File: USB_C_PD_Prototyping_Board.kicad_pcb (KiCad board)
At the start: 2 copper layers, 60 x 45 mm, 48 parts, among them IC1 TPS259474LRPWR, IC2 BD33FC0FP-E2, J1 USB_C_Receptacle, J2 Power_out, J3 Data_out, J5 Conn_01x04_Pin, J6 Conn_02x02_Counter_Clockwise, J7 Conn_02x02_Counter_Clockwise, Q1 DMP3018SFV-7, Q2 DMP3018SFV-7, SW1 Power_out_switch, U1 HUSB238_xxxDD

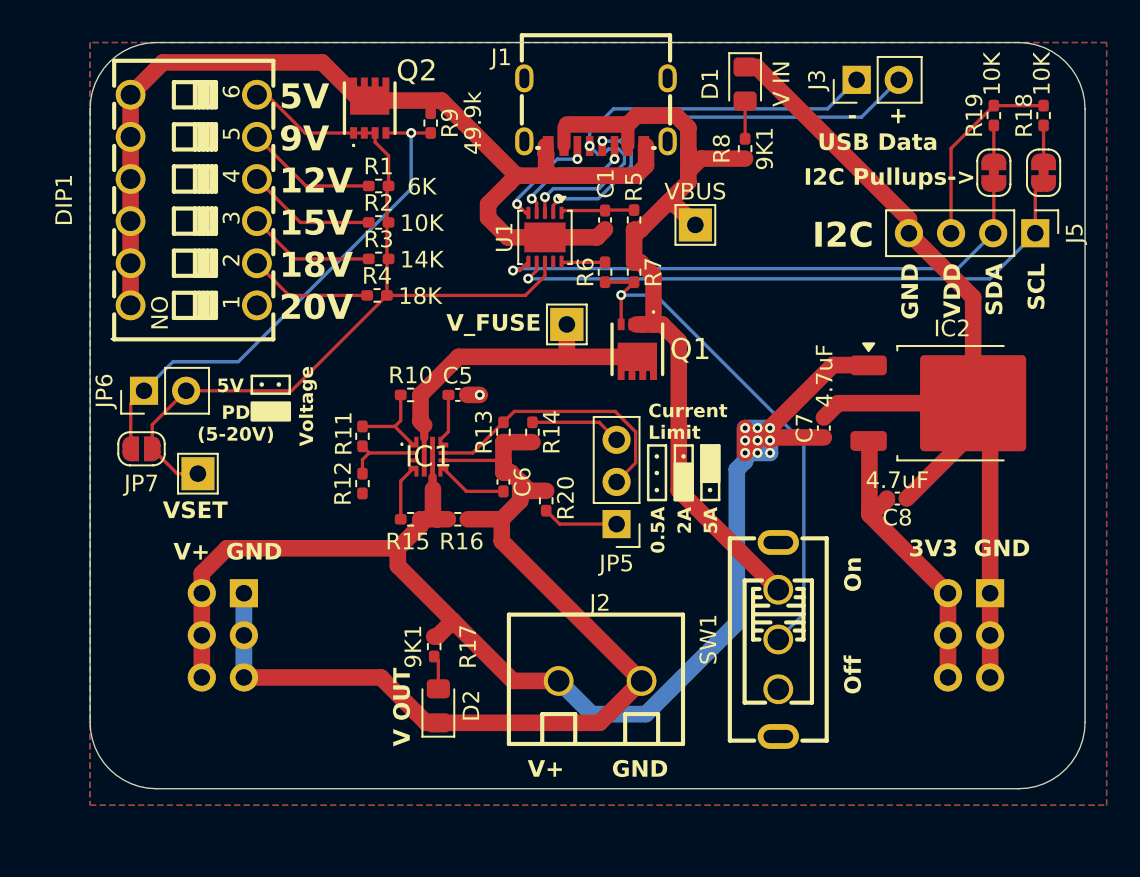
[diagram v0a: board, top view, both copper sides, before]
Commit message: Re-worked after initial tests
- Corrected silkscreen labels for output switch
- Corrected jumper logic polarity for voltage select
- Added ISET resistor to set default current request to 3A (instead of 3.25A for open circuit) so that 9, 12V selectable with DIP switches
- Double indicator LED limiting resistor values to reduce brightness
- Changed 3V3 reg to switch mode to solve thermals
- Added cutout to limit covering of breadboard rows
- Made as many resistors as possible THT to use as a soldering task (will spin up an SMD only one as a cheaper out of the box solution too)
- Simplified and thickened primary current path (there wasn't a problem, but it will be more capable now)
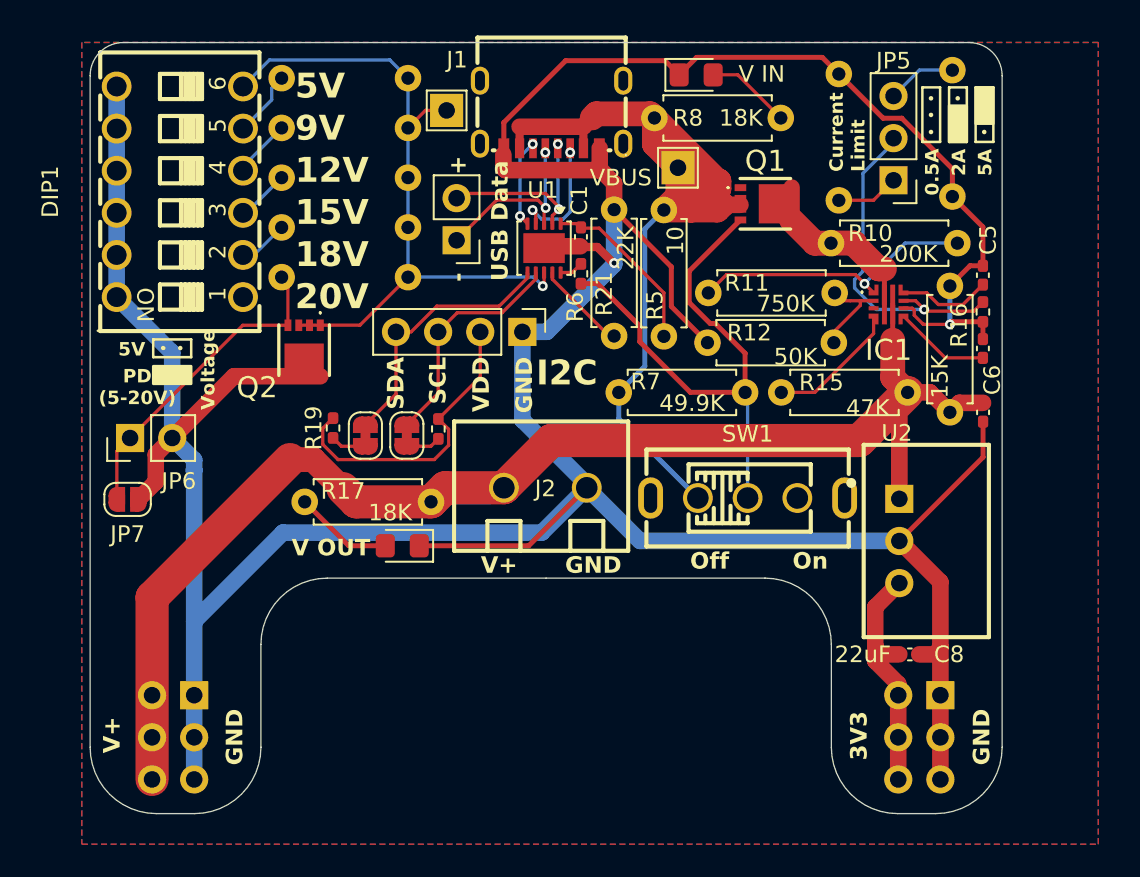
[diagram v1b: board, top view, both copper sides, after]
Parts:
- removed IC2: BD33FC0FP-E2, Package_TO_SOT_SMD:TO-252-2
- removed TP3: TESTPOINTROUND1.5MMNO, TestPoint:TestPoint_THTPad_2.0x2.0mm_Drill1.0mm
- added R21: 22K, Resistor_THT:R_Axial_DIN0207_L6.3mm_D2.5mm_P7.62mm_Horizontal, F.Cu at (43.6, 22.1)
- added U2: K7803-500R3_C909766, EasyEDA:PWRM-TH_K78XX-500R3, F.Cu at (60.8, 42.1)
- C7: value 4.7uF -> 10uF
- C8: value 4.7uF -> 22uF
- R1, R14, R2, R3, R4: footprint Resistor_SMD:R_0402_1005Metric_Pad0.72x0.64mm_HandSolder -> Resistor_THT:R_Axial_DIN0207_L6.3mm_D2.5mm_P7.62mm_Horizontal; moved to B.Cu
- R10: value 200k -> 200K; footprint Resistor_SMD:R_0402_1005Metric_Pad0.72x0.64mm_HandSolder -> Resistor_THT:R_Axial_DIN0207_L6.3mm_D2.5mm_P7.62mm_Horizontal
- R11: value 750k -> 750K; footprint Resistor_SMD:R_0402_1005Metric_Pad0.72x0.64mm_HandSolder -> Resistor_THT:R_Axial_DIN0207_L6.3mm_D2.5mm_P7.62mm_Horizontal
- R12: value 50k -> 50K; footprint Resistor_SMD:R_0402_1005Metric_Pad0.72x0.64mm_HandSolder -> Resistor_THT:R_Axial_DIN0207_L6.3mm_D2.5mm_P7.62mm_Horizontal
- R13: value 6.49k -> 6.49K
- R15: value 47k -> 47K; footprint Resistor_SMD:R_0402_1005Metric_Pad0.72x0.64mm_HandSolder -> Resistor_THT:R_Axial_DIN0207_L6.3mm_D2.5mm_P7.62mm_Horizontal
- R16: value 15k -> 15K; footprint Resistor_SMD:R_0402_1005Metric_Pad0.72x0.64mm_HandSolder -> Resistor_THT:R_Axial_DIN0207_L6.3mm_D2.5mm_P7.62mm_Horizontal
- R17, R8: value 9K1 -> 18K; footprint Resistor_SMD:R_0402_1005Metric_Pad0.72x0.64mm_HandSolder -> Resistor_THT:R_Axial_DIN0207_L6.3mm_D2.5mm_P7.62mm_Horizontal
- R20: value 2.2k -> 2K2; footprint Resistor_SMD:R_0402_1005Metric_Pad0.72x0.64mm_HandSolder -> Resistor_THT:R_Axial_DIN0207_L6.3mm_D2.5mm_P7.62mm_Horizontal; moved to B.Cu
- R5: footprint Resistor_SMD:R_0402_1005Metric_Pad0.72x0.64mm_HandSolder -> Resistor_THT:R_Axial_DIN0207_L6.3mm_D2.5mm_P7.62mm_Horizontal
- R6: value 5.1k -> 5.1K
- R7: value 49.9k -> 49.9K; footprint Resistor_SMD:R_0402_1005Metric_Pad0.72x0.64mm_HandSolder -> Resistor_THT:R_Axial_DIN0207_L6.3mm_D2.5mm_P7.62mm_Horizontal
- R9: value 49.9k -> 49.9K; footprint Resistor_SMD:R_0402_1005Metric_Pad0.72x0.64mm_HandSolder -> Resistor_THT:R_Axial_DIN0207_L6.3mm_D2.5mm_P7.62mm_Horizontal; moved to B.Cu
- moved R19 44.1 mm to (26.6, 35.2)
- moved JP4 41.5 mm to (31.1, 35.7), turned to -90 degrees
- moved R18 41.1 mm to (33.0, 35.3)
- moved JP1 41.1 mm to (28.6, 35.7), turned to -90 degrees
- moved R10 34.2 mm to (64.3, 24.1), turned to 180 degrees
- moved R14 33.4 mm to (64.0, 13.7)
- moved C5 32.5 mm to (65.8, 26.0), turned to -90 degrees
- moved J5 31.5 mm to (38.1, 29.4)
- moved R16 30.4 mm to (63.8, 34.3), turned to 90 degrees
- moved C6 30.0 mm to (65.8, 30.4)
- moved R13 29.8 mm to (65.8, 28.2)
- moved IC1 29.2 mm to (60.1, 27.8)
- moved JP5 26.6 mm to (60.5, 20.3)
- moved TP1 26.5 mm to (33.5, 16.1)
- moved J3 26.0 mm to (34.1, 23.9), turned to 180 degrees
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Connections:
- C7 pad 1: VOUT -> GND
- C7 pad 2: GND -> VOUT
- DIP1 pad 12: Net-(JP6-B) -> Net-(U1-VSET)
- J5 pad 1: SCL -> GND
- J5 pad 2: SDA -> VDD
- J5 pad 3: VDD -> SCL
- J5 pad 4: GND -> SDA
- JP6 pad 2: Net-(JP6-B) -> GND
- JP7 pad 2: Net-(JP6-B) -> GND
- Q1 pad 1: VBUS -> (no net)
- Q2 pad 1: Net-(JP6-B) -> Net-(U1-VSET)
- Q2 pad 2: Net-(JP6-B) -> Net-(U1-VSET)
- Q2 pad 3: Net-(JP6-B) -> Net-(U1-VSET)
- R1 pad 2: Net-(JP6-B) -> Net-(U1-VSET)
- R2 pad 2: Net-(JP6-B) -> Net-(U1-VSET)
- R3 pad 2: Net-(JP6-B) -> Net-(U1-VSET)
- R4 pad 2: Net-(JP6-B) -> Net-(U1-VSET)
- R9 pad 1: GND -> Net-(JP6-A)
- R9 pad 2: Net-(JP6-A) -> Net-(U1-VSET)
- TP1 pad 1: Net-(JP6-B) -> Net-(U1-VSET)
- U1 pad 8: Net-(JP6-B) -> Net-(U1-VSET)
- U1 pad 9: unconnected-(U1-ISET-Pad9) -> Net-(U1-ISET)
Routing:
- net GND: track 182.3 -> 242.4 mm, vias 1 -> 2
- net Net-(JP6-B): track 51.8 -> 0.00 mm
- net Net-(U1-VSET): track 0.00 -> 42.8 mm, vias 0 -> 1
- net SCL: track 36.2 -> 14.0 mm, vias 1 -> 0
- net SDA: track 34.1 -> 16.0 mm, vias 1 -> 0
- net D-: track 27.9 -> 11.1 mm
- net D+: track 27.4 -> 11.8 mm
- net /UVLO: track 5.59 -> 17.5 mm, vias 0 -> 1
- net Net-(JP6-A): track 31.1 -> 19.4 mm, vias 1 -> 0
- net VBUS: track 51.4 -> 61.4 mm
- net VFuse: track 18.2 -> 10.7 mm
- net VDD: track 11.8 -> 18.3 mm
- net Net-(U1-VIN): track 4.45 -> 10.6 mm
- net Net-(U1-ISET): track 0.00 -> 5.54 mm
- net /PGTH: track 3.39 -> 8.09 mm
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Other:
- board size 60 x 45 mm -> 55 x 46.5 mm
- board text added: "+"
- board text added: "-"
- board text added: "3V3"
- board text added: "USB Data"
- board text added: "V+"
- board text removed: "- + USB Data"
- board text removed: "3V3 GND"
- board text removed: "I2C Pullups->"
- board text removed: "VSET"
- board text removed: "V_FUSE"

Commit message: Seperate hand solder and ready to use versions
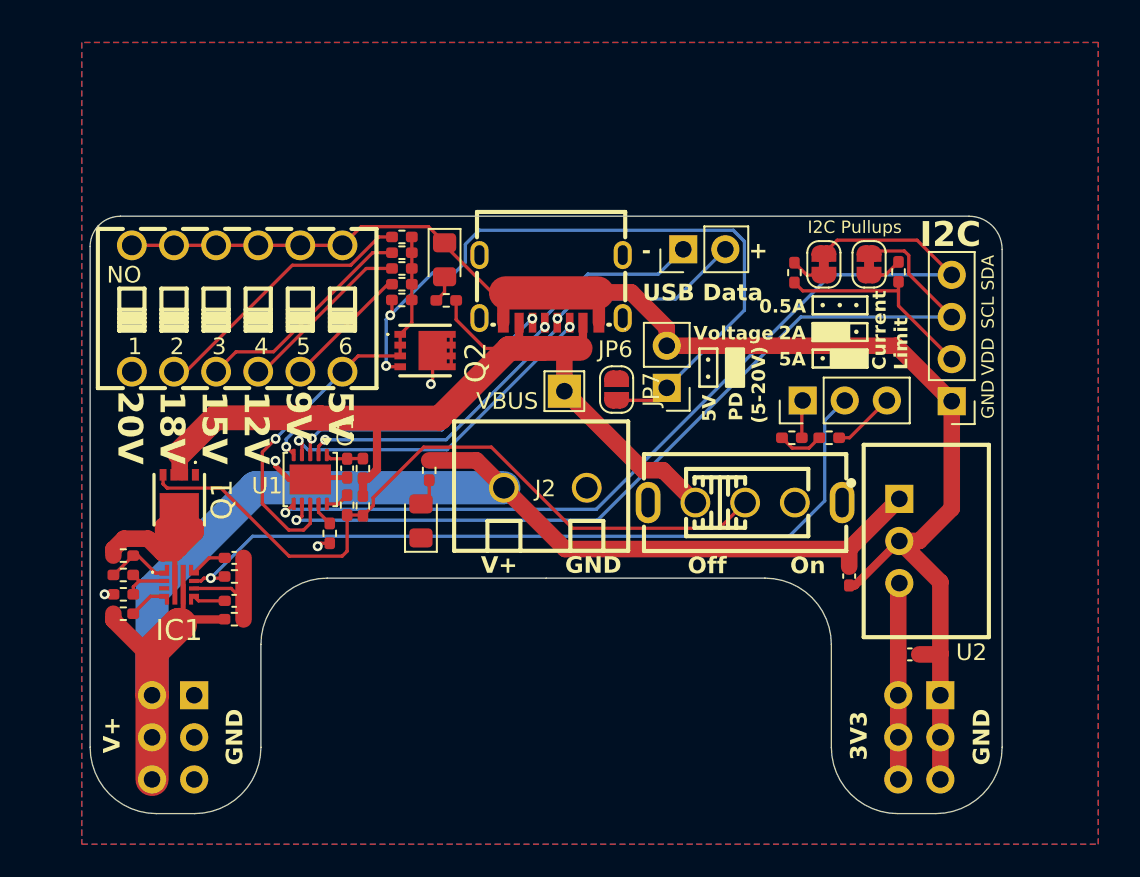
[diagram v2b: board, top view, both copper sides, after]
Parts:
- removed TP1: TESTPOINTROUND1.5MMNO, TestPoint:TestPoint_THTPad_2.0x2.0mm_Drill1.0mm
- R1, R14, R2, R20, R3, R4, R9: footprint Resistor_THT:R_Axial_DIN0207_L6.3mm_D2.5mm_P7.62mm_Horizontal -> Resistor_SMD:R_0402_1005Metric_Pad0.72x0.64mm_HandSolder; moved to F.Cu
- R10, R11, R12, R15, R16, R17, R21, R5, R7, R8: footprint Resistor_THT:R_Axial_DIN0207_L6.3mm_D2.5mm_P7.62mm_Horizontal -> Resistor_SMD:R_0402_1005Metric_Pad0.72x0.64mm_HandSolder
- moved R10 53.7 mm to (14.0, 42.9)
- moved C5 48.3 mm to (20.7, 43.1), turned to 180 degrees
- moved R13 47.9 mm to (20.7, 44.2), turned to 180 degrees
- moved C6 47.7 mm to (20.7, 45.7), turned to 180 degrees
- moved IC1 46.0 mm to (17.4, 44.7)
- moved R16 44.9 mm to (20.7, 46.8), turned to 0 degrees
- moved R15 41.9 mm to (14.0, 46.4), turned to 180 degrees
- moved Q1 39.6 mm to (17.4, 39.6), turned to 180 degrees
- moved R11 39.2 mm to (14.0, 44.1)
- moved R12 38.4 mm to (14.0, 45.3)
- moved JP6 32.5 mm to (46.8, 32.8), turned to 180 degrees
- moved JP7 30.2 mm to (43.8, 32.9), turned to 90 degrees
- moved JP4 29.7 mm to (59.0, 25.4)
- moved JP1 29.5 mm to (56.2, 25.4)
- moved R19 29.4 mm to (54.5, 25.9), turned to -90 degrees
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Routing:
- net GND: track 242.4 -> 108.6 mm, vias 2 -> 4
- net SDA: track 16.0 -> 55.8 mm, vias 0 -> 1
- net SCL: track 14.0 -> 53.1 mm, vias 0 -> 1
- net Net-(IC1-ILM): track 20.3 -> 47.5 mm
- net Net-(JP6-A): track 19.4 -> 43.5 mm, vias 0 -> 2
- net D+: track 11.8 -> 30.3 mm
- net D-: track 11.1 -> 28.3 mm
- net Net-(U1-VSET): track 42.8 -> 26.2 mm
- net CC2: track 5.32 -> 19.0 mm
- net /UVLO: track 17.5 -> 3.98 mm, vias 1 -> 0
- net Net-(DIP1-Pad8): track 3.02 -> 16.5 mm
- net CC1: track 7.17 -> 20.5 mm
- net Net-(Q1-G): track 32.9 -> 44.4 mm
- net Net-(DIP1-Pad9): track 3.21 -> 13.6 mm
- net Net-(U1-VIN): track 10.6 -> 2.27 mm
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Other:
- board size 55 x 46.5 mm -> 55 x 36 mm
- board text added: "(5-20V)"
- board text added: "I2C Pullups"
- board text added: "PD"
- board text removed: "PD (5-20V)"
- board text removed: "V IN"
- board text removed: "V OUT"
